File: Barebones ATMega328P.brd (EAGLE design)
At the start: 160 x 100 mm, 3 parts, among them IC1 ATMEGA328P-AU

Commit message: v. 0.9
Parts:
- removed CN1: (no value), adafruit:DCJACK_2MM_PTH
- added 5V-CON, GND-CON, PWR-IN: PINHD-1X3, Connector:1X03
- added C1, C2: 10uF, rcl:E5-8,5
- added C3, C4: 22pF, rcl:C025-025X050
- added C5: 1uF, rcl:E5-8,5
- added IC2: 7805TV, linear:TO220V
- added JP1: PINHD-1X7, Connector:1X07
- added JP2: PINHD-1X6, Connector:1X06
- added LED1: RED, led:LED3MM
- added LED2: GREEN, led:LED3MM
- added Q1: (no value), adafruit:HC49/S
- added R1: 220R, rcl:0207/10
- added R2: 1K, rcl:0207/10
- added R3: 10k, rcl:0207/10
- added R4: 0R, rcl:0207/10
- added SW1: 1-1825910-3, Switches:SW4_1825910-D
- moved IC1 34.4 mm to (12.7, 25.7), flipped to the bottom, turned to 90 degrees
- moved ICSP 27.6 mm to (7.87, 40.4), turned to 180 degrees
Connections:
- removed net AVCC: IC1.18
- removed net GNDBREAK: CN1.GNDBREAK
- removed net PWR: CN1.PWR
- new net (PCINT10/ADC2)PC2: IC1.25, JP1.4
- new net (PCINT11/ADC3)PC3: IC1.26, JP1.5
- new net (PCINT12/SDA/ADC4)PC4: IC1.27, JP1.6
- new net (PCINT13/SCL/ADC5)PC5: IC1.28, JP1.7
- new net (PCINT8/ADC0)PC0: IC1.23, JP1.2
- new net (PCINT9/ADC1)PC1: IC1.24, JP1.3
- new net 10: IC1.10, JP2.2
- new net 11: IC1.11, JP2.3
- new net 12: IC1.12, JP2.4
- new net 13: IC1.13, JP2.5
- new net 14: IC1.14, JP2.6
- new net 9: IC1.9, JP2.1
- new net ADC7: IC1.22, JP1.1
- new net MISO: IC1.16, ICSP.1
- new net MOSI: IC1.15, ICSP.4
- new net N$1: LED1.A, R1.1
- new net N$2: R3.1, SW1.4
- new net N$3: C5.-, IC1.29, SW1.3
- new net N$4: ICSP.2, R4.1
- new net N$5: LED2.A, R2.2
- new net PB6: C4.2, IC1.7, Q1.2
- new net PB7: C3.2, IC1.8, Q1.1
- new net RESET: C5.+, ICSP.5
- new net SCK: IC1.17, ICSP.3, R2.1
- new net VIN: C1.+, IC2.1, PWR-IN.1
- net GND: now also C1.-, C2.-, C3.1, C4.1, GND-CON.1, GND-CON.2, GND-CON.3, IC2.2, ICSP.6, LED1.K, LED2.K, PWR-IN.3, SW1.1; no longer CN1.GND
- net VCC: now also 5V-CON.1, 5V-CON.2, 5V-CON.3, C2.+, IC1.18, IC2.3, R1.2, R3.2, R4.2
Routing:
- net GND: track 0.00 -> 194.4 mm
- net VCC: track 0.00 -> 90.1 mm
- net RESET: track 0.00 -> 44.8 mm
- net N$3: track 0.00 -> 21.8 mm
- net (PCINT13/SCL/ADC5)PC5: track 0.00 -> 20.1 mm
- net SCK: track 0.00 -> 19.2 mm
- net VIN: track 0.00 -> 17.8 mm
- net (PCINT12/SDA/ADC4)PC4: track 0.00 -> 17.2 mm
- net MISO: track 0.00 -> 15.5 mm
- net (PCINT11/ADC3)PC3: track 0.00 -> 14.4 mm
- net MOSI: track 0.00 -> 14.2 mm
- net PB6: track 0.00 -> 13.0 mm
- net PB7: track 0.00 -> 12.1 mm
- net (PCINT10/ADC2)PC2: track 0.00 -> 11.5 mm
- net (PCINT9/ADC1)PC1: track 0.00 -> 11.2 mm
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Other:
- board size 160 x 100 mm -> 47 x 45.7 mm

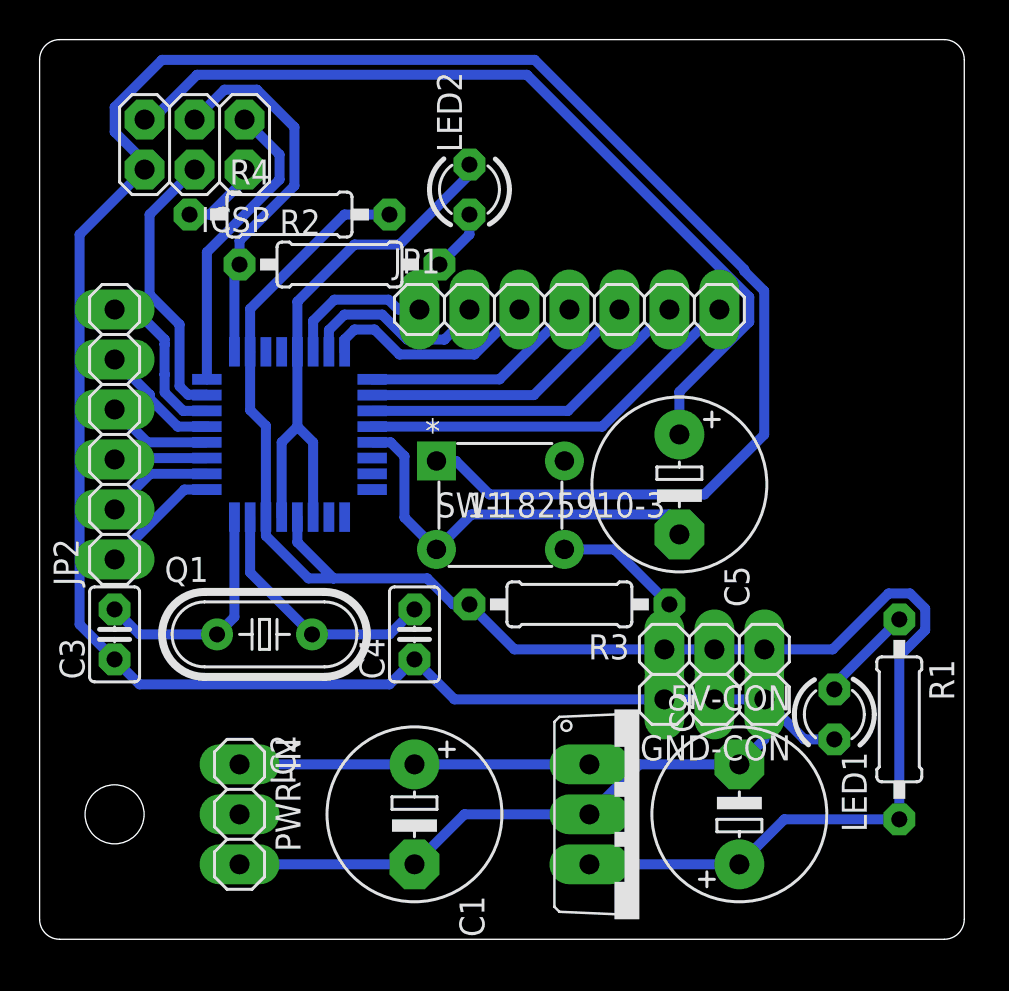
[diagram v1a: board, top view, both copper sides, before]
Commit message: Moved Power LED, made board footprint smaller
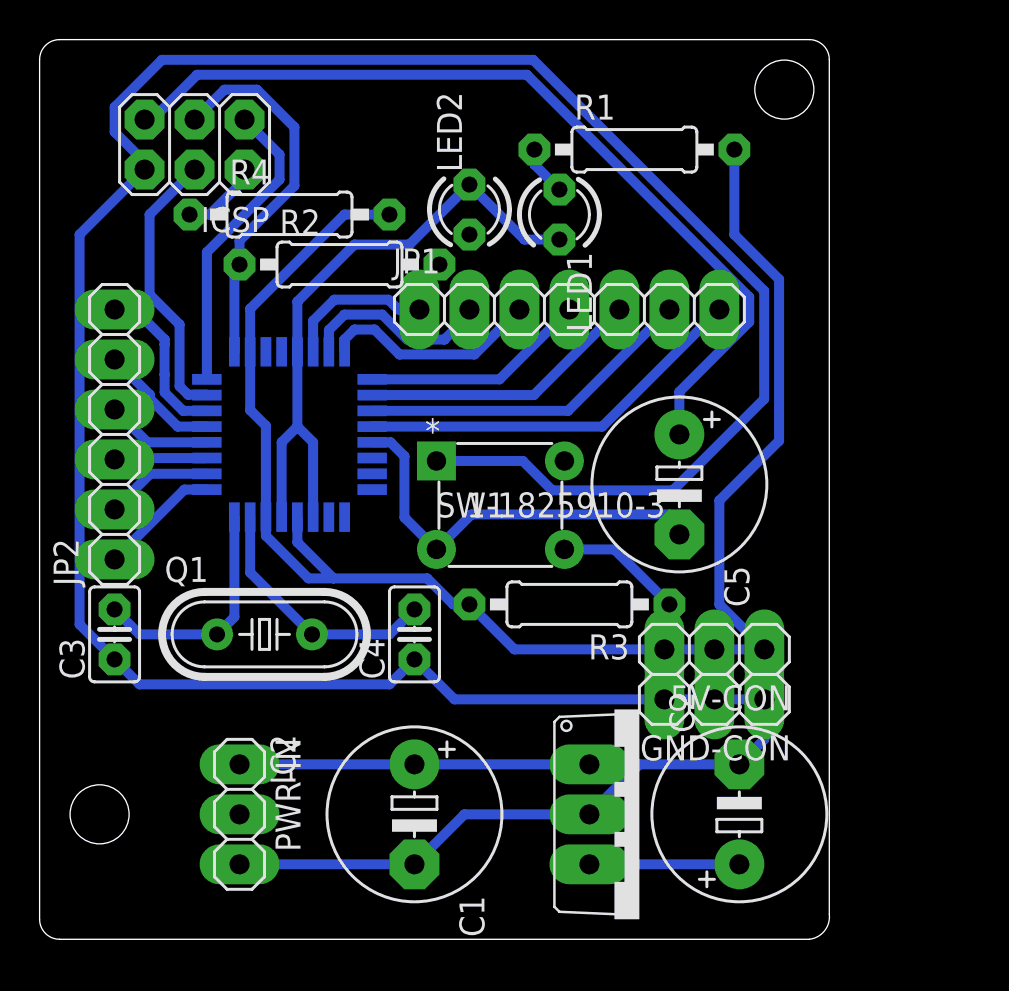
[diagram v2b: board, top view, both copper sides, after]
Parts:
- moved R1 31.9 mm to (30.2, 40.1), turned to 0 degrees
- moved LED1 29.0 mm to (26.4, 36.8)
- moved LED2 1.02 mm to (21.8, 37.1)
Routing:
- net N$5: track 3.17 -> 0.00 mm
- net N$1: track 4.92 -> 2.56 mm
- net VCC: track 90.1 -> 88.7 mm
- net GND: track 194.4 -> 193.8 mm
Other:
- board size 47 x 45.7 mm -> 40.1 x 45.7 mm
